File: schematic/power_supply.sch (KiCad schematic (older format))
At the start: 55 parts, among them J1 CONN_01X02, J2 CONN_01X01, J3 CONN_01X01, J4 CONN_01X01, J5 CONN_01X01, J6 CONN_01X01, Q1 Q_PMOS_GSD, U1 MCP1726-3302E/SN, U2 MCP1612, U3 MCP1726-3302E/SN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

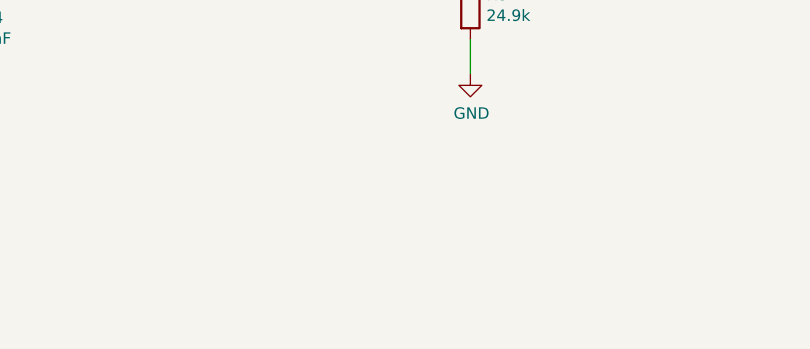
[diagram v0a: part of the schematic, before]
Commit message: Moved all references to F.Fab, cleaned up silkscreen
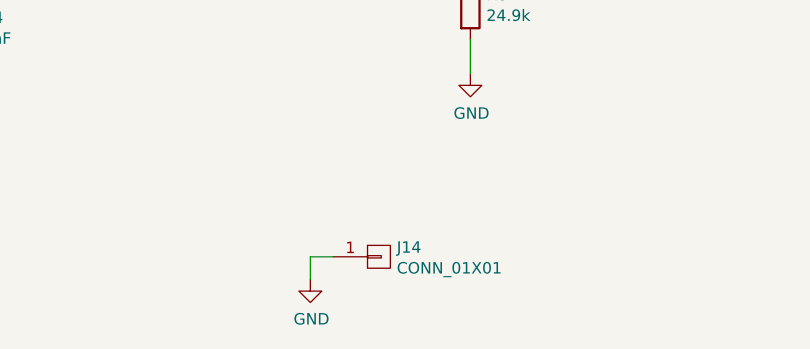
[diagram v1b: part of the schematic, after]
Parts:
- added J14: CONN_01X01, Pin_Headers:Pin_Header_Straight_1x01_Pitch2.54mm, symbol CONN_01X01
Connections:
- net GND: now also J14.1 (P1)
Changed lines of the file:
@@
 Wire Wire Line
 	4900 2450 5250 2450
+$Comp
+L CONN_01X01 J14
+U 1 1 59EC06AD
+P 4050 6750
+F 0 "J14" H 4128 6791 50  0000 L CNN
+F 1 "CONN_01X01" H 4128 6700 50  0000 L CNN
+F 2 "Pin_Headers:Pin_Header_Straight_1x01_Pitch2.54mm" H 4050 6750 50  0001 C CNN
+F 3 "" H 4050 6750 50  0001 C CNN
+	1    4050 6750
+	1    0    0    -1
+$EndComp
+$Comp
+L GND #PWR0162
+U 1 1 59EC0BAF
+P 3750 6850
+F 0 "#PWR0162" H 3750 6600 50  0001 C CNN
+F 1 "GND" H 3755 6677 50  0000 C CNN
+F 2 "" H 3750 6850 50  0001 C CNN
+F 3 "" H 3750 6850 50  0001 C CNN
+	1    3750 6850
+	1    0    0    -1
+$EndComp
+Wire Wire Line
+	3750 6850 3750 6750
+Wire Wire Line
+	3750 6750 3850 6750
 $EndSCHEMATC
